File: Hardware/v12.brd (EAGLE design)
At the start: 50 x 50 mm, 82 parts, among them IC1 LM324D, IC2 m328p, IC3 REG1117, IC4 OPA336U, J1 22-27-2081-08, J2 22-27-2031-03

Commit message: slight changes
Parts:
- moved OPAMP-C4 0.33 mm to (45.0, 15.3)
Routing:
- net BUTTON_+: track 63.0 -> 61.5 mm
- net DISP_2: track 22.7 -> 22.1 mm

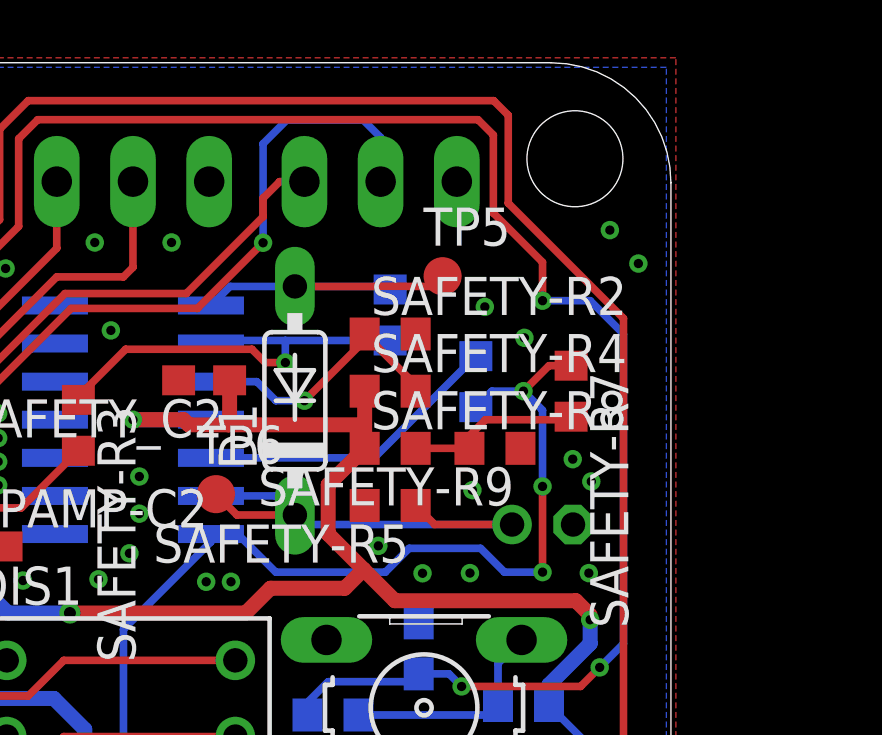
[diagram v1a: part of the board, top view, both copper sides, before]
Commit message: changed diode to a minimelf diode from open parts library
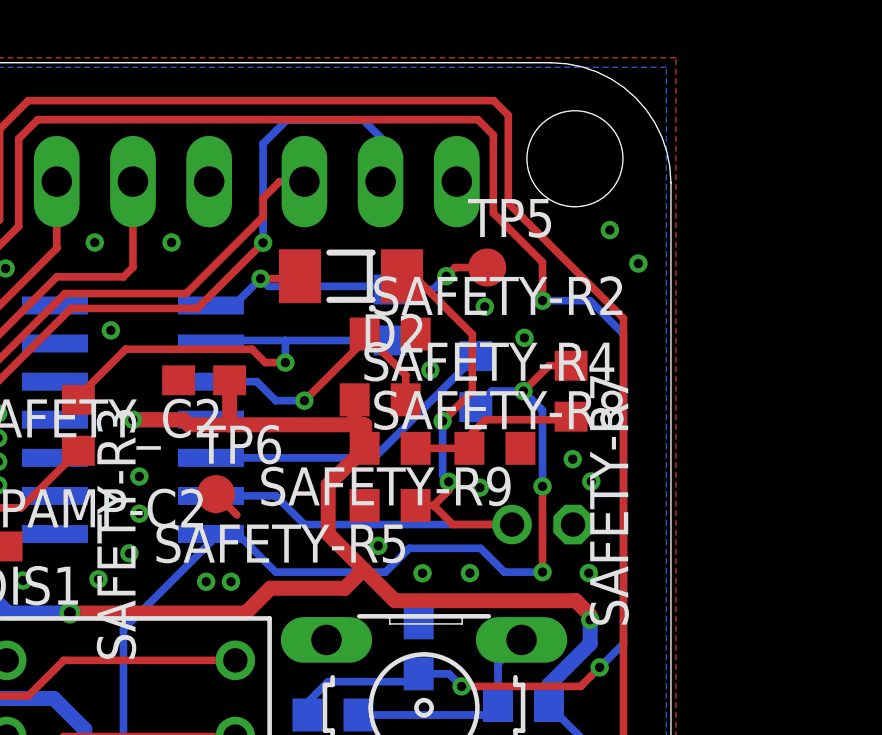
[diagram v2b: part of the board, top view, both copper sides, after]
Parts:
- removed D1: 1N4148DO35-7, diode:DO35-7
- added D2: LL4148, _hhn_diodes_smd:SOD80_DO213AA_MINIMELF
- moved TP5 1.51 mm to (43.9, 43.2)
- moved SAFETY-R4 0.44 mm to (40.3, 38.8)
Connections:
- net N$11: now also D2.C; no longer D1.C
- net N$7: now also D2.A; no longer D1.A
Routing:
- net N$11: track 16.8 -> 24.9 mm, vias 0 -> 2
- net N$7: track 11.3 -> 11.4 mm, vias 0 -> 2
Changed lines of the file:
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@@
 <param name="mdDrill" value="10mil"/>
 <param name="mdSmdStop" value="0mil"/>
-<param name="msWidth" value="8mil"/>
+<param name="msWidth" value="6mil"/>
 <param name="msDrill" value="12mil"/>
 <param name="msMicroVia" value="12mil"/>
@@
 <element name="AVR-L1" library="rcl" package="L2825P" value="10u" x="20.0025" y="29.845" rot="MR270"/>
 <element name="AVR-R1" library="rcl" package="R0603" value="10k" x="7.540625" y="44.92625" rot="R270"/>
-<element name="D1" library="diode" package="DO35-7" value="1N4148DO35-7" x="37.465" y="38.735" rot="R90"/>
 <element name="DIS1" library="display-hp" package="HDSP-E" value="SC39-11SRWA" x="31.67" y="25">
 <attribute name="OC_NEWARK" value="unknown" x="31.67" y="25" size="1.778" layer="27" display="off"/>
@@
 <element name="SAFETY-R2" library="rcl" package="R0603" value="100k" x="40.64" y="40.9575"/>
 <element name="SAFETY-R3" library="rcl" package="R0603" value="20k" x="30.248225" y="37.91585" rot="R270"/>
-<element name="SAFETY-R4" library="rcl" package="R0603" value="68k" x="40.64" y="39.0525"/>
+<element name="SAFETY-R4" library="rcl" package="R0603" value="68k" x="40.3098" y="38.763575"/>
 <element name="SAFETY-R5" library="rcl" package="R0603" value="220k" x="40.64" y="35.2425" rot="R180"/>
 <element name="SAFETY-R6" library="rcl" package="R0603" value="200k" x="43.4975" y="39.37" rot="MR270"/>
@@
 <attribute name="TP_SIGNAL_NAME" value="" x="30.667325" y="19.605625" size="1.778" layer="28" rot="MR0" display="off"/>
 </element>
-<element name="TP5" library="testpad" package="B1,27" value="TPB1,27" x="42.389425" y="42.884725">
-<attribute name="TP_SIGNAL_NAME" value="" x="42.389425" y="42.884725" size="1.778" layer="27" display="off"/>
+<element name="TP5" library="testpad" package="B1,27" value="TPB1,27" x="43.875325" y="43.17365">
+<attribute name="TP_SIGNAL_NAME" value="" x="43.875325" y="43.17365" size="1.778" layer="27" display="off"/>
 </element>
 <element name="TP6" library="testpad" package="B1,27" value="TPB1,27" x="34.8361" y="35.620325">
@@
 <attribute name="TP_SIGNAL_NAME" value="" x="35.57905" y="17.789525" size="1.778" layer="27" display="off"/>
 </element>
+<element name="D2" library="_hhn_diodes_smd" package="SOD80_DO213AA_MINIMELF" value="LL4148" x="39.335075" y="42.884725" rot="R180"/>
 </elements>
 <signals>
@@
 <wire x1="32.0675" y1="38.1" x2="34.6675" y2="38.1" width="0.5" layer="16"/>
 <wire x1="39.79" y1="37.1475" x2="39.79" y2="37.931725" width="0.5" layer="1"/>
-<wire x1="39.79" y1="37.931725" x2="39.79" y2="39.0525" width="0.5" layer="1"/>
 <wire x1="21.0375" y1="42.7101" x2="21.0375" y2="41.1925" width="0.5" layer="1"/>
 <wire x1="21.0375" y1="41.1925" x2="21.2725" y2="40.9575" width="0.5" layer="1"/>
@@
 <wire x1="33.925775" y1="37.931725" x2="35.24885" y2="37.931725" width="0.5" layer="1"/>
 <via x="11.820525" y="16.309975" extent="1-16" drill="0.31"/>
-<wire x1="35.24885" y1="37.931725" x2="39.79" y2="37.931725" width="0.5" layer="1"/>
+<wire x1="35.24885" y1="37.931725" x2="39.417625" y2="37.931725" width="0.5" layer="1"/>
+<wire x1="39.417625" y1="37.931725" x2="39.79" y2="37.931725" width="0.5" layer="1"/>
 <wire x1="11.820525" y1="16.309975" x2="12.887325" y2="17.376775" width="0.5" layer="16"/>
 <wire x1="12.887325" y1="17.376775" x2="18.161" y2="17.376775" width="0.5" layer="16"/>
@@
 <wire x1="45.881025" y1="15.27175" x2="46.00485" y2="15.395575" width="0.5" layer="1"/>
 <wire x1="46.00485" y1="15.395575" x2="47.672625" y2="15.395575" width="0.5" layer="1"/>
+<wire x1="39.4598" y1="38.763575" x2="39.4598" y2="37.9739" width="0.5" layer="1"/>
+<wire x1="39.4598" y1="37.9739" x2="39.417625" y2="37.931725" width="0.5" layer="1"/>
 </signal>
 <signal name="GND">
@@
 <via x="43.30065" y="32.98825" extent="1-16" drill="0.31"/>
 <via x="47.3456" y="36.0426" extent="1-16" drill="0.31"/>
-<via x="43.3832" y="35.753675" extent="1-16" drill="0.31"/>
+<via x="43.63085" y="35.836225" extent="1-16" drill="0.31"/>
 <via x="43.79595" y="41.862375" extent="1-16" drill="0.31"/>
 <via x="33.353375" y="44.008675" extent="1-16" drill="0.31"/>
@@
 <via x="46.726475" y="36.78555" extent="1-16" drill="0.31"/>
 <via x="47.26305" y="32.98825" extent="1-16" drill="0.31"/>
+<via x="41.97985" y="39.75735" extent="1-16" drill="0.31"/>
 </signal>
 <signal name="N$1">
@@
 <contactref element="IC1" pad="1"/>
 <contactref element="SAFETY-R1" pad="1"/>
-<contactref element="D1" pad="A"/>
-<wire x1="34.6675" y1="41.91" x2="35.3025" y2="42.545" width="0.254" layer="16"/>
-<wire x1="35.3025" y1="42.545" x2="37.465" y2="42.545" width="0.254" layer="16"/>
 <wire x1="40.64" y1="42.4425" x2="40.5375" y2="42.545" width="0.254" layer="16"/>
-<wire x1="40.5375" y1="42.545" x2="37.465" y2="42.545" width="0.254" layer="16"/>
 <contactref element="TP5" pad="TP"/>
-<wire x1="42.389425" y1="42.884725" x2="42.0497" y2="42.545" width="0.254" layer="1"/>
-<wire x1="42.0497" y1="42.545" x2="37.465" y2="42.545" width="0.254" layer="1"/>
+<contactref element="D2" pad="A"/>
+<wire x1="34.6675" y1="41.91" x2="35.429825" y2="41.91" width="0.254" layer="16"/>
+<wire x1="35.429825" y1="41.91" x2="36.322" y2="42.802175" width="0.254" layer="16"/>
+<via x="36.322" y="42.802175" extent="1-16" drill="0.31"/>
+<wire x1="36.322" y1="42.802175" x2="37.552525" y2="42.802175" width="0.254" layer="1"/>
+<wire x1="37.552525" y1="42.802175" x2="37.635075" y2="42.884725" width="0.254" layer="1"/>
+<wire x1="40.5375" y1="42.545" x2="36.579175" y2="42.545" width="0.254" layer="16"/>
+<wire x1="36.579175" y1="42.545" x2="36.322" y2="42.802175" width="0.254" layer="16"/>
+<wire x1="43.875325" y1="43.17365" x2="42.802175" y2="43.17365" width="0.254" layer="1"/>
+<wire x1="42.802175" y1="43.17365" x2="42.51325" y2="42.884725" width="0.254" layer="1"/>
+<via x="42.51325" y="42.884725" extent="1-16" drill="0.31"/>
+<wire x1="42.51325" y1="42.884725" x2="42.071025" y2="42.4425" width="0.254" layer="16"/>
+<wire x1="42.071025" y1="42.4425" x2="40.64" y2="42.4425" width="0.254" layer="16"/>
 </signal>
 <signal name="N$8">
@@
 <wire x1="37.7825" y1="38.735" x2="39.79" y2="40.7425" width="0.254" layer="1"/>
 <wire x1="39.79" y1="40.7425" x2="39.79" y2="40.9575" width="0.254" layer="1"/>
-<wire x1="39.79" y1="40.9575" x2="41.49" y2="39.2575" width="0.254" layer="1"/>
-<wire x1="41.49" y1="39.2575" x2="41.49" y2="39.0525" width="0.254" layer="1"/>
+<wire x1="41.1598" y1="38.763575" x2="41.1598" y2="39.5877" width="0.254" layer="1"/>
+<wire x1="41.1598" y1="39.5877" x2="39.79" y2="40.9575" width="0.254" layer="1"/>
 </signal>
 <signal name="N$11">
-<contactref element="D1" pad="C"/>
 <contactref element="SAFETY_C1" pad="+"/>
 <contactref element="SAFETY-R5" pad="1"/>
 <contactref element="IC1" pad="6"/>
 <wire x1="34.6675" y1="35.56" x2="36.83" y2="35.56" width="0.254" layer="16"/>
-<wire x1="36.83" y1="35.56" x2="37.465" y2="34.925" width="0.254" layer="16"/>
 <wire x1="44.704" y1="34.6075" x2="37.7825" y2="34.6075" width="0.254" layer="16"/>
-<wire x1="37.7825" y1="34.6075" x2="37.465" y2="34.925" width="0.254" layer="16"/>
-<wire x1="44.704" y1="34.6075" x2="42.125" y2="34.6075" width="0.254" layer="1"/>
-<wire x1="42.125" y1="34.6075" x2="41.49" y2="35.2425" width="0.254" layer="1"/>
 <contactref element="TP6" pad="TP"/>
 <wire x1="34.8361" y1="35.620325" x2="35.531425" y2="34.925" width="0.254" layer="1"/>
-<wire x1="35.531425" y1="34.925" x2="37.465" y2="34.925" width="0.254" layer="1"/>
+<contactref element="D2" pad="C"/>
+<wire x1="36.83" y1="35.56" x2="37.7825" y2="34.6075" width="0.254" layer="16"/>
+<wire x1="41.035075" y1="42.884725" x2="41.4401" y2="42.884725" width="0.254" layer="1"/>
+<wire x1="41.4401" y1="42.884725" x2="43.380025" y2="40.9448" width="0.254" layer="1"/>
+<wire x1="42.719625" y1="38.38575" x2="42.389425" y2="38.05555" width="0.254" layer="1"/>
+<via x="42.389425" y="38.05555" extent="1-16" drill="0.31"/>
+<wire x1="42.389425" y1="38.05555" x2="42.389425" y2="36.23945" width="0.254" layer="16"/>
+<wire x1="42.389425" y1="36.23945" x2="42.5958" y2="36.033075" width="0.254" layer="16"/>
+<via x="42.5958" y="36.033075" extent="1-16" drill="0.31"/>
+<wire x1="42.5958" y1="36.033075" x2="42.5958" y2="35.74415" width="0.254" layer="1"/>
+<wire x1="42.5958" y1="35.74415" x2="42.09415" y2="35.2425" width="0.254" layer="1"/>
+<wire x1="42.09415" y1="35.2425" x2="41.49" y2="35.2425" width="0.254" layer="1"/>
+<wire x1="44.704" y1="34.6075" x2="42.72915" y2="34.6075" width="0.254" layer="1"/>
+<wire x1="42.72915" y1="34.6075" x2="42.09415" y2="35.2425" width="0.254" layer="1"/>
+<wire x1="43.380025" y1="40.9448" x2="43.380025" y2="39.04615" width="0.254" layer="1"/>
+<wire x1="43.380025" y1="39.04615" x2="42.389425" y2="38.05555" width="0.254" layer="1"/>
+<wire x1="34.8361" y1="35.620325" x2="34.6675" y2="35.56" width="0" layer="19" extent="1-16"/>
 </signal>
 <signal name="N$12">

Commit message: slight renaming for better understanding
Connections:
- removed net DISP_0: DISP-Q3.1, IC2.11
- removed net ENABLE_LED_0: DIS1.3, DIS1.8, DISP-Q3.3
- new net DISP_3: DISP-Q1.1, IC2.9
- new net ENABLE_LED_3: DIS3.3, DIS3.8, DISP-Q1.3
- net DISP_1: now also DISP-Q3.1, IC2.11; no longer DISP-Q2.1, IC2.10
- net DISP_2: now also DISP-Q2.1, IC2.10; no longer DISP-Q1.1, IC2.9
- net ENABLE_LED_1: now also DIS1.3, DIS1.8, DISP-Q3.3; no longer DIS2.3, DIS2.8, DISP-Q2.3
- net ENABLE_LED_2: now also DIS2.3, DIS2.8, DISP-Q2.3; no longer DIS3.3, DIS3.8, DISP-Q1.3
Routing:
- net ENABLE_LED_0: track 30.1 -> 0.00 mm, vias 1 -> 0
- net DISP_3: track 0.00 -> 22.1 mm, vias 0 -> 3
- net DISP_2: track 22.1 -> 9.56 mm, vias 3 -> 1
- net ENABLE_LED_3: track 0.00 -> 11.6 mm
- net ENABLE_LED_2: track 11.6 -> 22.7 mm, vias 0 -> 1
- net ENABLE_LED_1: track 22.7 -> 30.1 mm
- net DISP_0: track 6.03 -> 0.00 mm, vias 1 -> 0
- net DISP_1: track 9.56 -> 6.03 mm
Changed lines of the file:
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@@
 <wire x1="39.633525" y1="4.365625" x2="39.633525" y2="3.508375" width="0.5" layer="16"/>
 </signal>
-<signal name="ENABLE_LED_1">
+<signal name="ENABLE_LED_2">
 <contactref element="DISP-Q2" pad="3"/>
 <contactref element="DIS2" pad="3"/>
@@
 <wire x1="9.695" y1="33.734375" x2="9.525" y2="33.904375" width="0.254" layer="16"/>
 </signal>
-<signal name="ENABLE_LED_2">
+<signal name="ENABLE_LED_3">
 <contactref element="DISP-Q1" pad="3"/>
 <contactref element="DIS3" pad="8"/>
@@
 <wire x1="9.763125" y1="27.703125" x2="7.06" y2="25" width="0.254" layer="16"/>
 </signal>
-<signal name="ENABLE_LED_0">
+<signal name="ENABLE_LED_1">
 <contactref element="DISP-Q3" pad="3"/>
 <contactref element="DIS1" pad="3"/>
@@
 <wire x1="15.243125" y1="38.8175" x2="16.3449" y2="38.8175" width="0.254" layer="1"/>
 </signal>
-<signal name="DISP_0">
+<signal name="DISP_1">
 <contactref element="DISP-Q3" pad="1"/>
 <contactref element="IC2" pad="11"/>
@@
 <wire x1="14.8525" y1="39.6175" x2="16.3449" y2="39.6175" width="0.254" layer="1"/>
 </signal>
-<signal name="DISP_2">
+<signal name="DISP_3">
 <contactref element="DISP-Q1" pad="1"/>
 <contactref element="IC2" pad="9"/>
@@
 <wire x1="31.4824" y1="6.35635" x2="32.004" y2="6.87795" width="0.254" layer="16"/>
 </signal>
-<signal name="DISP_1">
+<signal name="DISP_2">
 <contactref element="DISP-Q2" pad="1"/>
 <contactref element="IC2" pad="10"/>

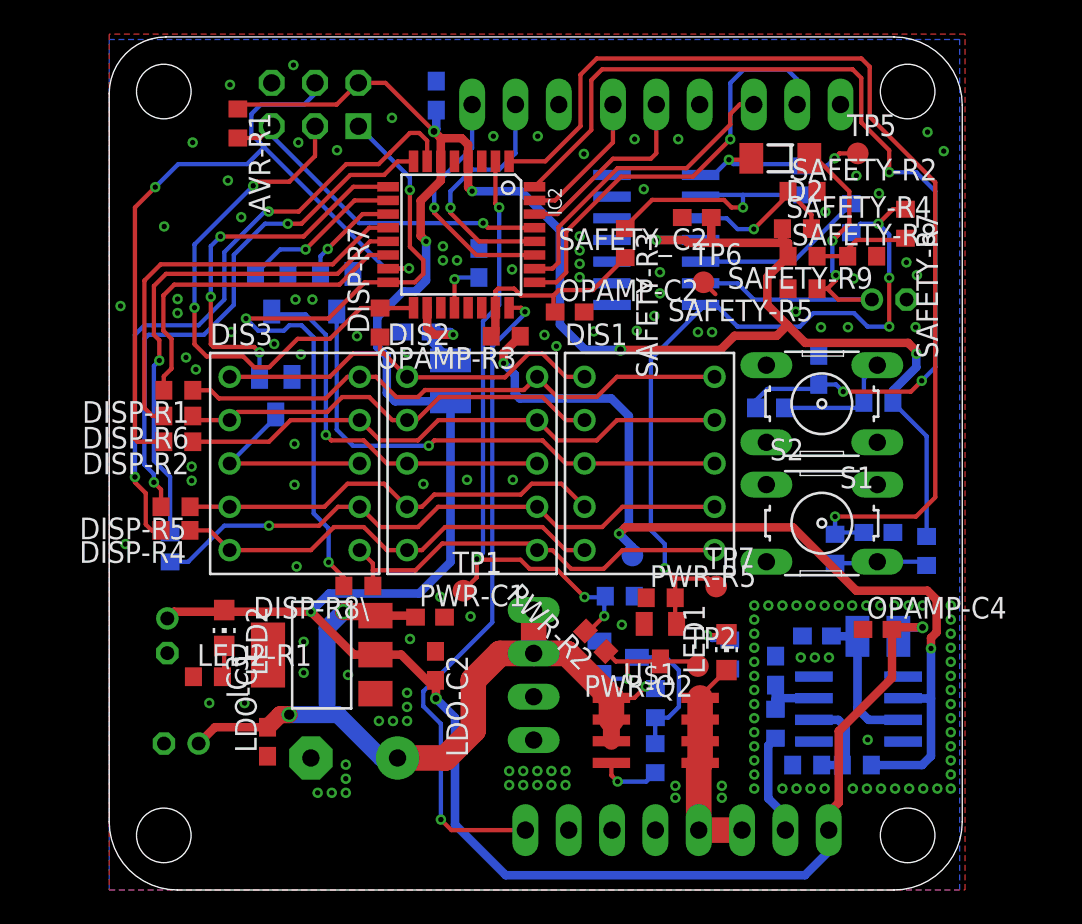
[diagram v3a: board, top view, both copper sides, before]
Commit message: added silk screen to test points and optimized ground connections
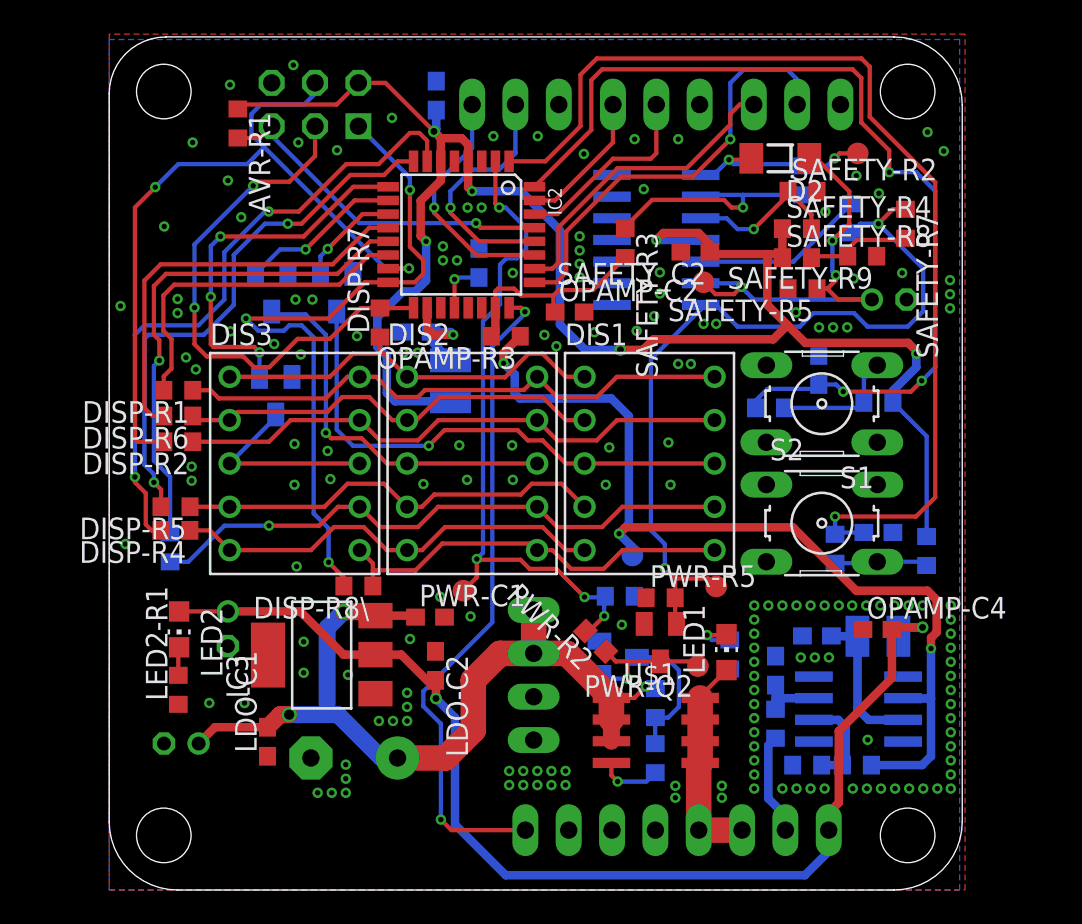
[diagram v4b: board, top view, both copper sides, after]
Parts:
- moved LDO-C3 3.57 mm to (6.96, 15.3)
- moved LED2 2.64 mm to (4.10, 15.3)
- moved SAFETY_C2 2.02 mm to (34.4, 37.4)
- moved LED2-R1 1.90 mm to (4.05, 11.7), turned to 90 degrees
- moved SAFETY-R8 0.34 mm to (40.3, 37.1)
- renumbered TP1 to LOET, TP2 to PWR_ENABLE, TP4 to TEMP_RAW, TP5 to SAFETY_1, TP6 to SAFETY_2, TP7 to SAFETY_3
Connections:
- net LOETKOLBEN_0 renamed LOETKOLBEN
- net N$10 renamed TX
- net N$13 renamed PC2
- net N$2 renamed SDA
- net N$3 renamed PC3
- net N$4 renamed SCL
- net N$9 renamed RX
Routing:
- net VCC: track 193.6 -> 172.7 mm, vias 9 -> 8
- net SAFETY: track 45.7 -> 48.0 mm, vias 4 -> 2
- net LOETKOLBEN: track 37.3 -> 39.1 mm
- net N$11: track 24.9 -> 26.6 mm, vias 2 -> 3
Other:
- board text added: "C3 C2 G"
- board text added: "DA CL G"
- board text added: "TX RX G"

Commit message: software readout of safety circuit additional led displaying state of safety circuit connecting soldering tip power switch to timer output OC0B
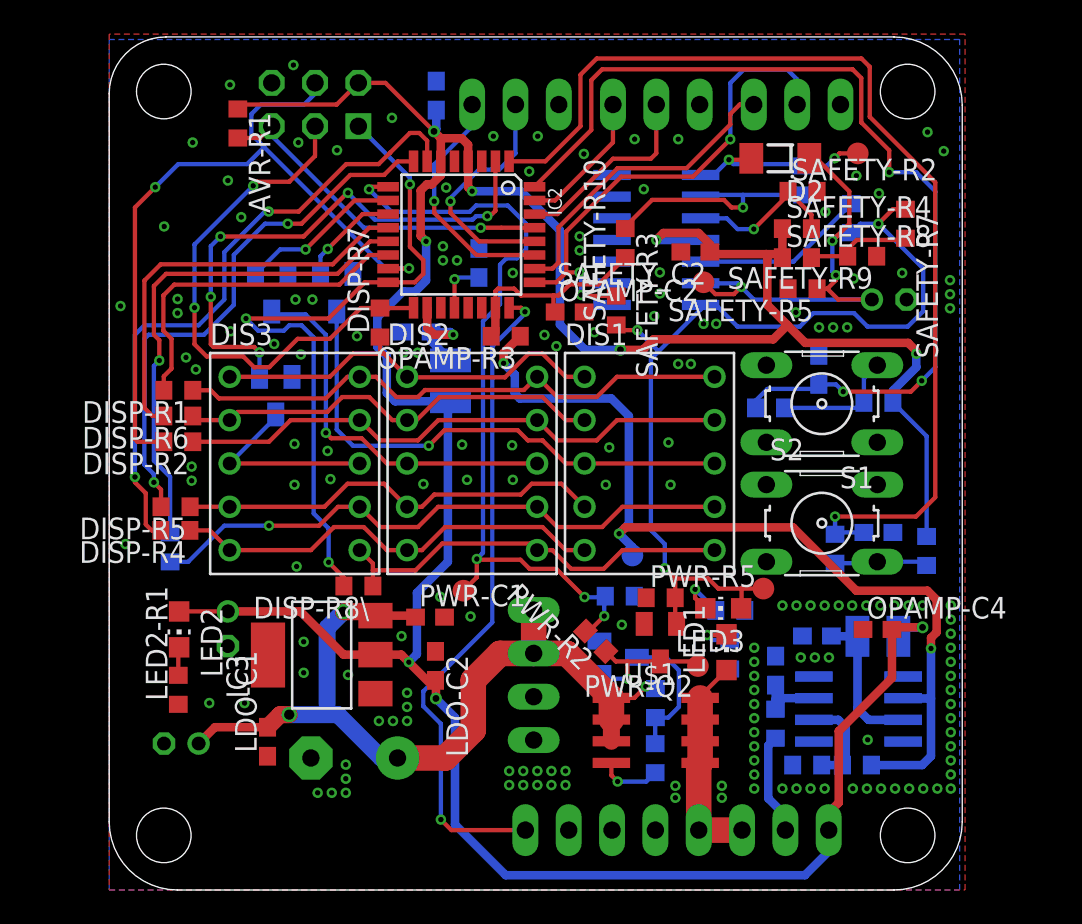
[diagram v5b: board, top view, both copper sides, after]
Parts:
- added LED3: GN, led:CHIP-LED0805
- added SAFETY-R10: 0 n.m., rcl:R0603
- added SAFETY-R11: 300, rcl:R0603
- LED2-R1: value 280 -> 300
- moved SAFETY_3 2.77 mm to (38.3, 17.7)
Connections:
- new net N$2: LED3.C, SAFETY-R11.1
- net DISP_3: now also IC2.2; no longer IC2.9
- net GND: now also SAFETY-R11.2
- net LOETKOLBEN: now also IC2.9; no longer IC2.2
- net PC2: now also SAFETY-R10.2
- net SAFETY: now also LED3.A, SAFETY-R10.1
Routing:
- net VCC: track 172.7 -> 189.1 mm, vias 8 -> 9
- net DISP_3: track 22.1 -> 32.0 mm, vias 3 -> 5
- net SAFETY: track 48.0 -> 55.1 mm, vias 2 -> 3
- net LOETKOLBEN: track 39.1 -> 46.1 mm
- net PC2: track 26.1 -> 30.3 mm, vias 1 -> 3
- net N$2: track 0.00 -> 3.10 mm, vias 0 -> 1
